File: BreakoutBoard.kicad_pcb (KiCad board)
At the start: 4 copper layers, 80 x 55 mm, 44 parts, among them J1 PJ-063AH, J10 10129381-906001BLF, J2 10129381-906001BLF, J3 10129381-906001BLF, J4 10129381-906001BLF, J5 RJHSE-5384, J6 10129381-906001BLF, J9 10129381-920001BLF, SW1 TS02-66-43, SW2 TS02-66-43, U1 AL5809-20S1-7, U2 LMR33620BDDA

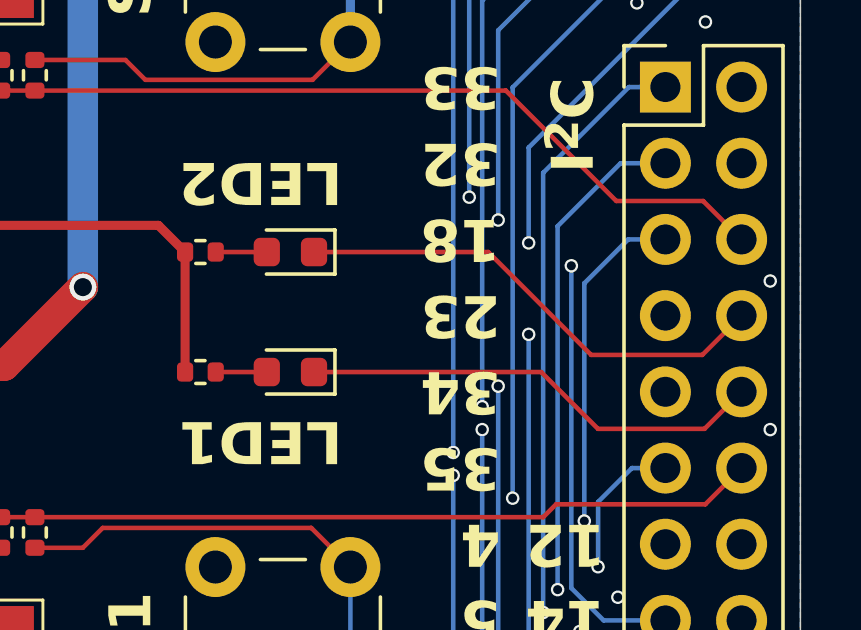
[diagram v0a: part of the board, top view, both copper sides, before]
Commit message: updated RJ45 connector part number and fixed silk screen mistakes on GPIO numbering
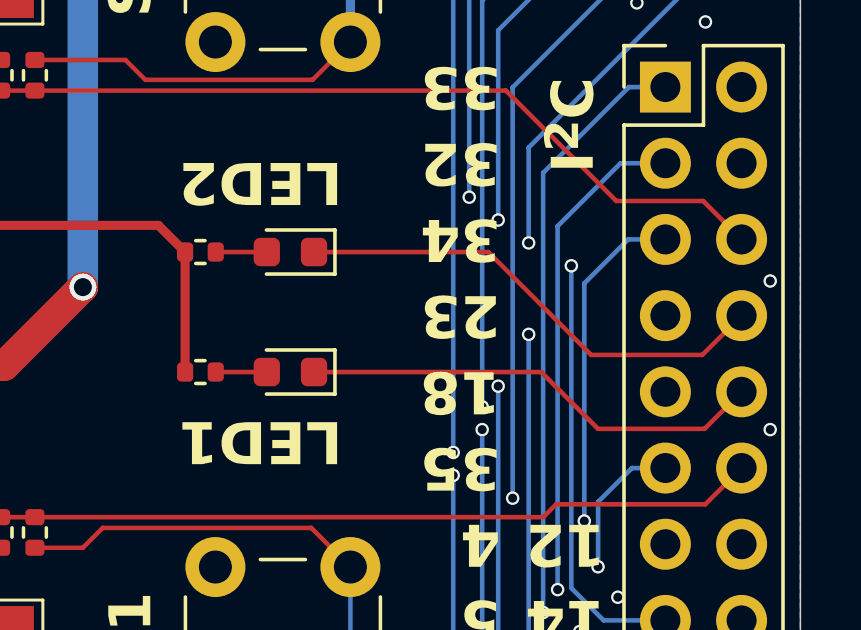
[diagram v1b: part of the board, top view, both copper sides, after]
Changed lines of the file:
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@@
 			)
 		)
-		(property "Datasheet" "~"
+		(property "Datasheet" "Data Sheets\\LS_Q976.01_EN.pdf"
 			(at 0 0 90)
 			(layer "F.Fab")
@@
 			)
 		)
-		(property "Datasheet" "~"
+		(property "Datasheet" "Data Sheets\\LS_Q976.01_EN.pdf"
 			(at 0 0 0)
 			(layer "F.Fab")
@@
 			)
 		)
-		(property "MOUSER#" "179-TS026643BK100SCR"
+		(property "MOUSER#" "179-TS026643BK100LCR"
 			(at 0 0 90)
 			(unlocked yes)
@@
 			)
 		)
-		(property "MOUSER#" "523-RJHSE-5384"
+		(property "MOUSER#" "523-RJHSE-5381"
 			(at 0 0 0)
 			(unlocked yes)
@@
 			)
 		)
-		(property "Datasheet" "~"
+		(property "Datasheet" "Data Sheets\\LS_Q976.01_EN.pdf"
 			(at 0 0 0)
 			(layer "F.Fab")
@@
 			)
 		)
-		(property "MOUSER#" "179-TS026643BK100SCR"
+		(property "MOUSER#" "179-TS026643BK100LCR"
 			(at 0 0 90)
 			(unlocked yes)
@@
 			)
 		)
-		(property "Datasheet" "~"
+		(property "Datasheet" "Data Sheets\\LS_Q976.01_EN.pdf"
 			(at 0 0 90)
 			(layer "F.Fab")
@@
 		)
 	)
-	(gr_text "34"
+	(gr_text "18"
 		(at 165 131.66 180)
 		(layer "F.SilkS" knockout)
@@
 		)
 	)
-	(gr_text "18"
+	(gr_text "34"
 		(at 165 126.58 180)
 		(layer "F.SilkS" knockout)

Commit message: added revision silkscreen text
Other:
- board text added: "REV ${REVISION}"
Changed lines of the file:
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@@
+		)
+	)
+	(gr_text "REV ${REVISION}"
+		(at 121 144 0)
+		(layer "B.SilkS" knockout)
+		(effects
+			(font
+				(size 1.4 1.4)
+				(thickness 0.28)
+				(bold yes)
+			)
+			(justify left mirror)
 		)
 	)

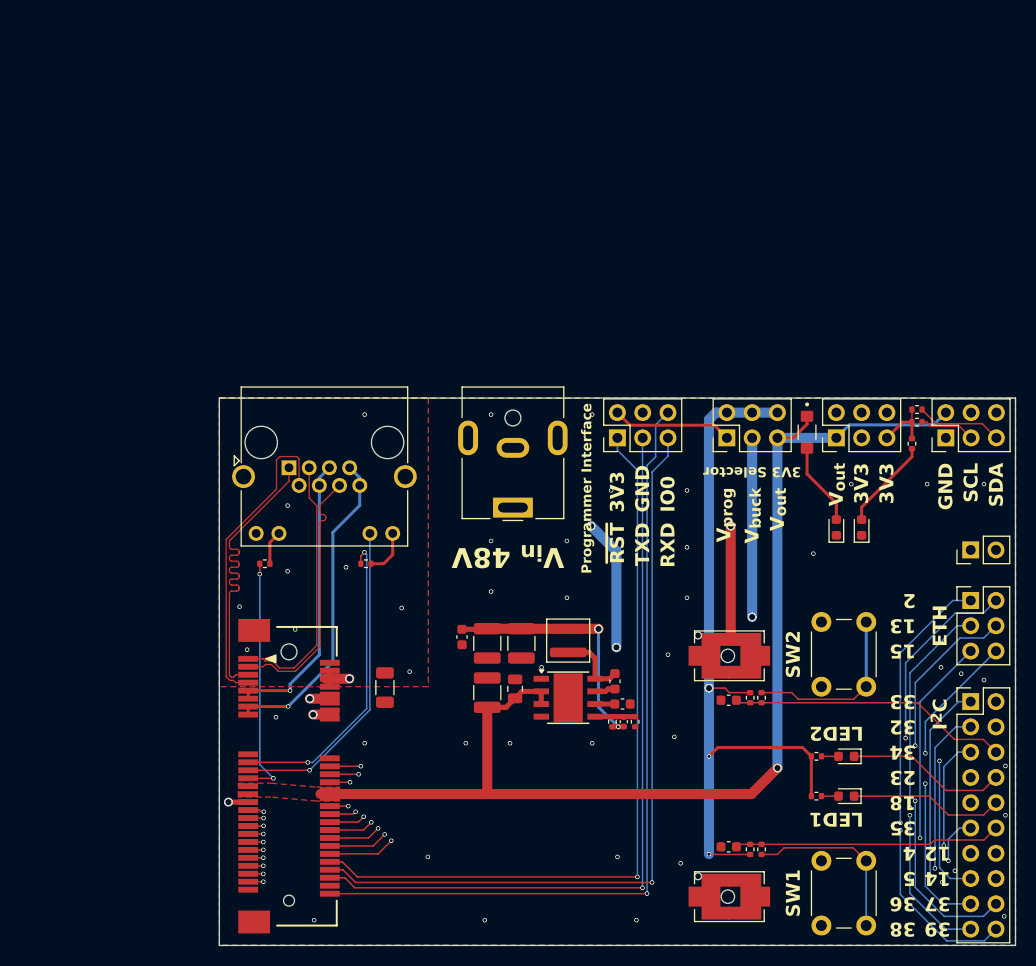
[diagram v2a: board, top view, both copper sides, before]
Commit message: completed routing for revision 0.2
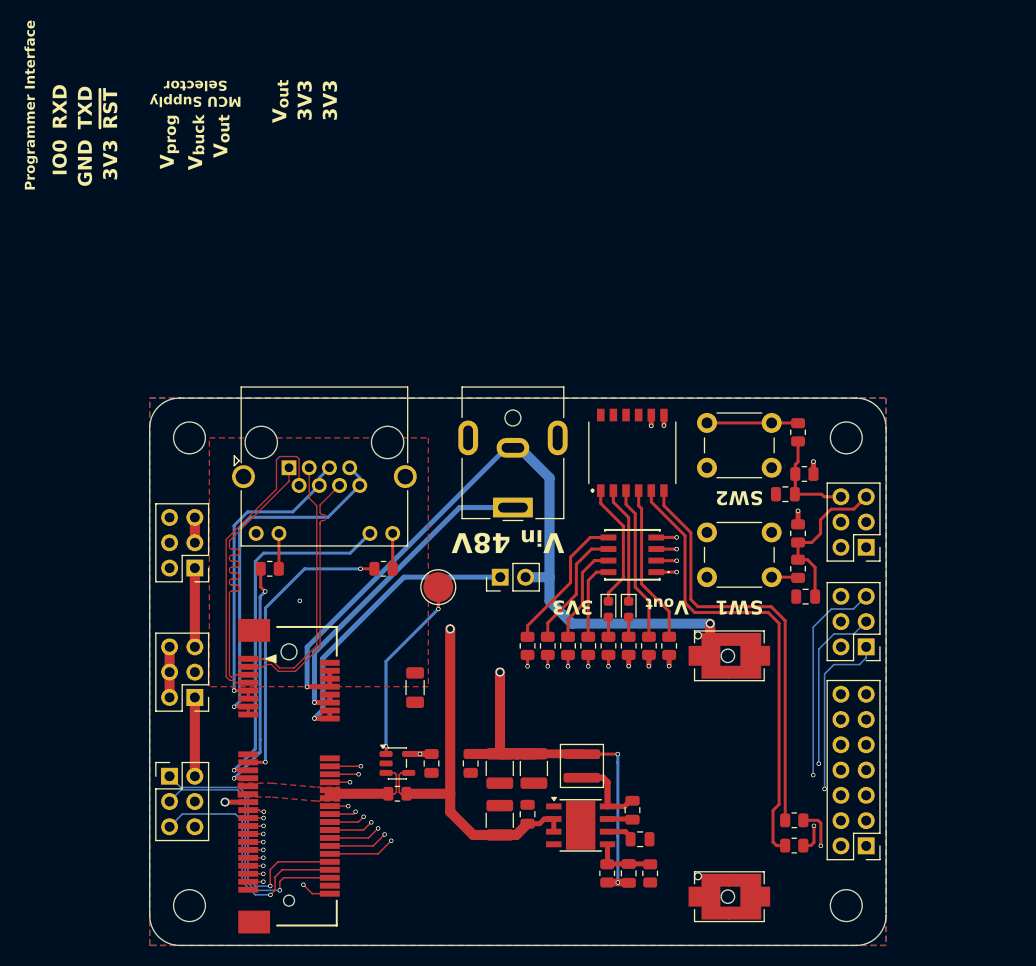
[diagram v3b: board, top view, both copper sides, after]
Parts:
- removed D1, D2: Red, LED_SMD:LED_0603_1608Metric
- added C12: 100nF, Capacitor_SMD:C_0805_2012Metric, F.Cu at (116.3, 127.7)
- added D5: Red, LED_SMD:LED_0603_1608Metric, F.Cu at (136.1, 112.2)
- added H1: MountingHole, MountingHole:MountingHole_3.2mm_M3, F.Cu at (92.0, 95.0)
- added H2: MountingHole, MountingHole:MountingHole_3.2mm_M3, F.Cu at (92.0, 142.0)
- added H3: MountingHole, MountingHole:MountingHole_3.2mm_M3, F.Cu at (158.0, 95.0)
- added H4: MountingHole, MountingHole:MountingHole_3.2mm_M3, F.Cu at (158.0, 142.0)
- added R14: 56R, Resistor_SMD:R_0805_2012Metric, F.Cu at (128.0, 115.9)
- added R15: 56R, Resistor_SMD:R_0805_2012Metric, F.Cu at (132.1, 115.9)
- added R16: 180R, Resistor_SMD:R_0805_2012Metric, F.Cu at (126.0, 115.9)
- added R17: 270R, Resistor_SMD:R_0805_2012Metric, F.Cu at (136.1, 115.9)
- added R18: 270R, Resistor_SMD:R_0805_2012Metric, F.Cu at (134.1, 115.9)
- added R19: 0R022, Resistor_SMD:R_0805_2012Metric, F.Cu at (112.9, 130.8)
- added SW4: GDH06S04, Project:GDH06S04, F.Cu at (136.5, 96.5)
- added TP1: TestPoint, TestPoint:TestPoint_Pad_D3.0mm, F.Cu at (117.0, 110.0)
- C10, C11, C4, C5, C9: footprint Capacitor_SMD:C_0603_1608Metric -> Capacitor_SMD:C_0805_2012Metric
- C6: footprint Capacitor_SMD:C_0402_1005Metric -> Capacitor_SMD:C_0805_2012Metric
- D3: value Red -> IN-P55QDTRGBW; footprint LED_SMD:LED_0603_1608Metric -> Project:INP55QDTRGBW
- J5: value RJHSE-5384 -> RJHSE-5381
- J9: value 10129381-920001BLF -> 10129381-914001BLF; footprint Connector_PinHeader_2.54mm:PinHeader_2x10_P2.54mm_Vertical -> Connector_PinHeader_2.54mm:PinHeader_2x07_P2.54mm_Vertical
- R1, R2: value 120R -> 270R; footprint Resistor_SMD:R_0402_1005Metric -> Resistor_SMD:R_0805_2012Metric
- R10, R11, R12, R13, R8, R9: footprint Resistor_SMD:R_0402_1005Metric -> Resistor_SMD:R_0805_2012Metric
- R3: value 120R -> 2K2; footprint Resistor_SMD:R_0402_1005Metric -> Resistor_SMD:R_0805_2012Metric
- R4: value 120R -> 100R 0.5W; footprint Resistor_SMD:R_0402_1005Metric -> Resistor_SMD:R_0805_2012Metric
- R5: value 10K -> 2K2; footprint Resistor_SMD:R_0402_1005Metric -> Resistor_SMD:R_0805_2012Metric
- R6: value 120R -> 56R 0.5W; footprint Resistor_SMD:R_0402_1005Metric -> Resistor_SMD:R_0805_2012Metric
- R7: value 10K -> 56R; footprint Resistor_SMD:R_0402_1005Metric -> Resistor_SMD:R_0805_2012Metric
- U1: value AL5809-20S1-7 -> INA180A2; footprint Project:SODFL3717X100N -> Package_TO_SOT_SMD:SOT-23-5
- moved J6 65.8 mm to (92.5, 108.1), turned to 180 degrees
- moved J3 59.5 mm to (92.5, 121.1), turned to 180 degrees
- moved J2 56.4 mm to (90.0, 129.0), turned to 0 degrees
- moved U1 52.9 mm to (112.9, 127.7), turned to 0 degrees
- moved J11 47.3 mm to (123.2, 109.0)
- moved R7 42.4 mm to (130.0, 115.9), turned to 90 degrees
- moved R3 42.1 mm to (152.8, 136.0), turned to 180 degrees
- moved R5 41.9 mm to (152.8, 133.4)
- moved SW1 41.1 mm to (144.0, 104.5), turned to 0 degrees
- moved D3 32.4 mm to (136.5, 106.8), turned to 90 degrees
- moved R11 32.1 mm to (153.2, 104.6), turned to -90 degrees
- moved R10 28.4 mm to (153.2, 108.2)
- moved D4 28.1 mm to (134.1, 112.2), turned to -90 degrees
- moved R12 26.9 mm to (153.2, 94.4)
- moved C10 26.3 mm to (153.9, 110.9)
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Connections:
- D3 pad 1: /LED1 -> Net-(D3-KW)
- D3 pad 2: Net-(D3-A) -> Net-(D3-KB)
- D4 pad 1: /LED2 -> Net-(D4-K)
- J10 pad 1: GND -> Net-(D3-KW)
- J10 pad 2: /V_{out} -> Net-(D3-KB)
- J10 pad 3: /SCL -> Net-(D3-KG)
- J10 pad 4: GND -> Net-(D3-KR)
- J10 pad 5: /SDA -> /SW1
- J10 pad 6: +3.3V -> /SW2
- J4 pad 1: /GPIO2 -> /GPIO15
- J4 pad 2: /PHY_EN -> /MDIO
- J4 pad 5: /GPIO15 -> /GPIO2
- J4 pad 6: /MDIO -> /PHY_EN
- J7 pad 25: /V_{out} -> /V_{out,h}
- J7 pad 26: /V_{out} -> /V_{out,h}
- J7 pad 27: /V_{out} -> /V_{out,h}
- J7 pad 28: /V_{out} -> /V_{out,h}
- J9 pad 1: /GPIO33 -> /GPIO14
- J9 pad 10: /LED1 -> /GPIO4
- J9 pad 11: /GPIO35 -> /GPIO36
- J9 pad 12: /SW1 -> /GPIO18
- J9 pad 13: /GPIO4 -> /GPIO23
- J9 pad 14: /GPIO12 -> /GPIO5
- J9 pad 2: /SDA -> /GPIO33
- J9 pad 4: /SCL -> /GPIO35
- J9 pad 5: /GPIO34 -> /GPIO12
- J9 pad 6: /SW2 -> /GPIO34
- J9 pad 7: /GPIO23 -> /GPIO39
- J9 pad 8: /LED2 -> /GPIO38
- J9 pad 9: /GPIO18 -> /GPIO37
- R1 pad 1: Net-(J5-Pad10) -> /ETH_LED1
- R1 pad 2: /ETH_LED1 -> Net-(J5-Pad10)
- R2 pad 1: Net-(J5-Pad12) -> /3V3A
- R2 pad 2: /3V3A -> Net-(J5-Pad12)
- R3 pad 1: +3.3V -> /GPIO32
- R4 pad 1: +3.3V -> Net-(R4-Pad1)
- R4 pad 2: Net-(D3-A) -> /V_{out}
- R5 pad 1: /SCL -> /GPIO33
- R5 pad 2: +3.3V -> Net-(R5-Pad2)
- R6 pad 1: +3.3V -> /V_{out}
- R6 pad 2: Net-(D4-A) -> Net-(R6-Pad2)
- R7 pad 1: /SDA -> +3.3V
- R7 pad 2: +3.3V -> Net-(D3-AB)
- U1 pad 1: /V_{out} -> Net-(TP1-Pad1)
- U1 pad 2: Net-(D2-A) -> GND
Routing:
- net +3.3V: track 165.5 -> 22.7 mm, vias 4 -> 11
- net /GPIO0: track 81.1 -> 19.5 mm
- net /RXD: track 78.2 -> 25.4 mm
- net /TXD: track 77.1 -> 26.7 mm
- net VDD: track 80.0 -> 29.9 mm
- net /~{RST}: track 76.5 -> 27.5 mm
- net Net-(R5-Pad2): track 0.00 -> 42.5 mm
- net /SCL: track 37.6 -> 0.00 mm
- net Net-(R3-Pad2): track 9.22 -> 46.6 mm
- net GNDPWR: track 113.9 -> 77.1 mm, vias 4 -> 2
- net /SDA: track 36.4 -> 0.00 mm
- net /GPIO33: track 92.3 -> 66.3 mm
- net Net-(D3-KG): track 0.00 -> 22.2 mm, vias 0 -> 1
- net Net-(D3-KW): track 0.00 -> 22.1 mm, vias 0 -> 1
- net /GPIO34: track 83.6 -> 61.8 mm, vias 2 -> 1
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- added copper zone on In2.Cu, net +3.3V
- added copper zone on F.Cu, net /V_{out,h}
- removed copper zone on F.Cu, net /V_{out}
- removed copper zone on In2.Cu, net Earth
- removed copper zone on In2.Cu, net GND
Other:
- board size 80 x 55 mm -> 74 x 55 mm
- board text added: "MCU Supply Selector"
- board text removed: "12"
- board text removed: "13"
- board text removed: "14"
- board text removed: "15"
- board text removed: "18"
- board text removed: "2"
- board text removed: "23"
- board text removed: "32"
- board text removed: "33"
- board text removed: "34"
- board text removed: "35"
- board text removed: "36"
- board text removed: "37"
- board text removed: "38"
- board text removed: "39"
- board text removed: "3V3 Selector"
- board text removed: "4"
- board text removed: "5"
- board text removed: "ETH"
- board text removed: "I^{2}C"
- board text removed: "LED1"
- board text removed: "LED2"
- board text removed: "MDC"
- board text removed: "MDIO"
- board text removed: "PHY_EN"
- board text removed: "PoE"
- board text removed: "SCL"
- board text removed: "SDA"
- board text removed: "V_{dd}"

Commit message: completed silk screen
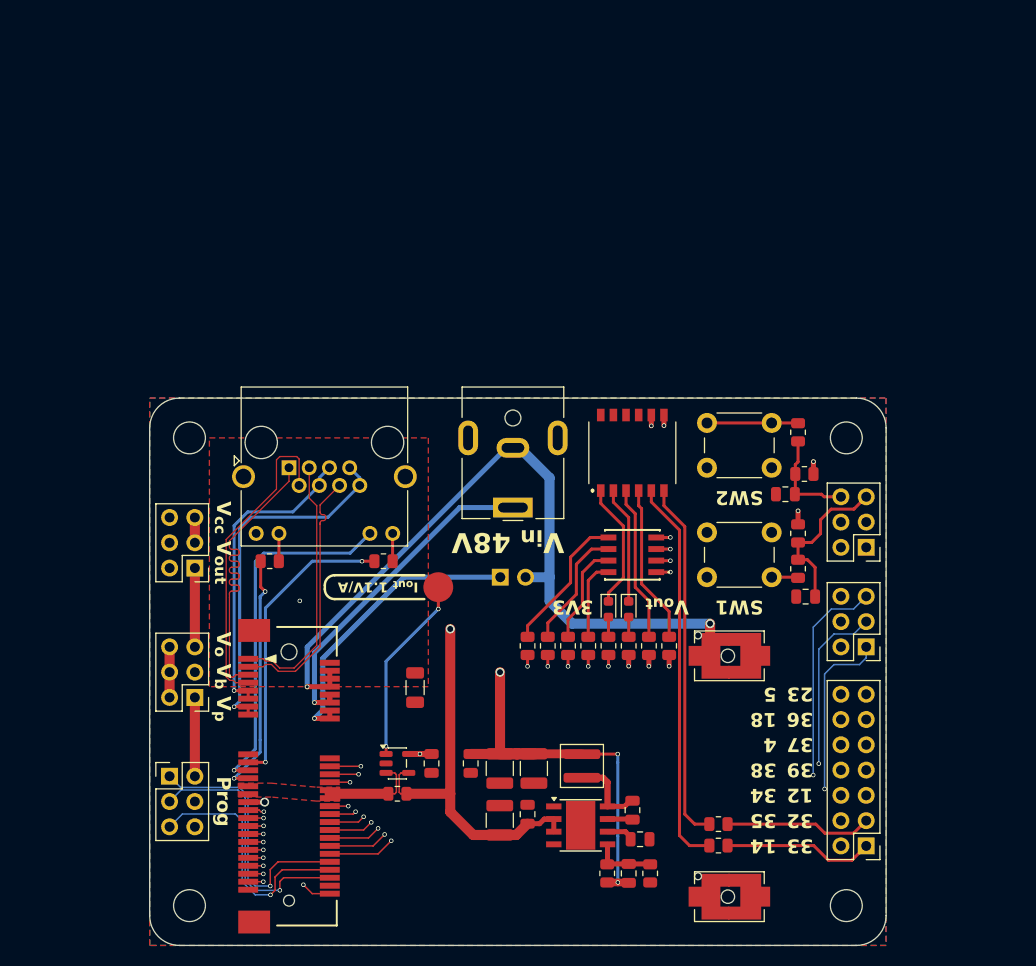
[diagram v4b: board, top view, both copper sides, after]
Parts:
- added G***: LOGO, LOGO, B.Cu at (121.0, 136.0)
- moved R5 7.63 mm to (145.2, 133.8)
- moved R3 7.62 mm to (145.2, 136.0)
- moved R1 0.76 mm to (100.1, 107.4)
- moved R2 0.76 mm to (111.5, 107.4)
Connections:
- J9 pad 1: /GPIO14 -> /GPIO33
- J9 pad 2: /GPIO33 -> /GPIO14
- R3 pad 1: /GPIO32 -> /GPIO33
- R5 pad 1: /GPIO33 -> /GPIO32
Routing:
- net /GPIO33: track 66.3 -> 79.9 mm, vias 2 -> 1
- net /GPIO32: track 67.4 -> 79.3 mm, vias 2 -> 1
- net Net-(R3-Pad2): track 46.6 -> 39.2 mm
- net Net-(R5-Pad2): track 42.5 -> 36.3 mm
- net /GPIO14: track 66.6 -> 62.3 mm
- net Net-(J5-Pad12): track 3.56 -> 2.80 mm
- net Net-(J5-Pad10): track 3.56 -> 2.80 mm
- net /ETH_LED1: track 24.0 -> 24.7 mm
- net +3.3V: track 22.7 -> 22.0 mm
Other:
- board text added: "12"
- board text added: "13"
- board text added: "14"
- board text added: "15"
- board text added: "18"
- board text added: "2"
- board text added: "23"
- board text added: "32"
- board text added: "33"
- board text added: "34"
- board text added: "35"
- board text added: "36"
- board text added: "37"
- board text added: "38"
- board text added: "39"
- board text added: "4"
- board text added: "5"
- board text added: "B"
- board text added: "EN"
- board text added: "G"
- board text added: "I_{out} 1.1V/A"
- board text added: "LED"
- board text added: "MDC"
- board text added: "MDIO"
- board text added: "PoE Supply"
- board text added: "Prog"
- board text added: "R"
- board text added: "V_{cc} V_{out}"
- board text added: "V_{dd} GND"
- board text added: "V_{o} V_{b} V_{p}"
- board text added: "W"
- board text removed: "Programmer Interface"
